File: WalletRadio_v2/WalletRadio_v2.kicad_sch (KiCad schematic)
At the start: 30 parts, among them Q1 BSP315P, Q2 Q_NPN_ECB, SW1 SW_SPDT, U3 LM324A

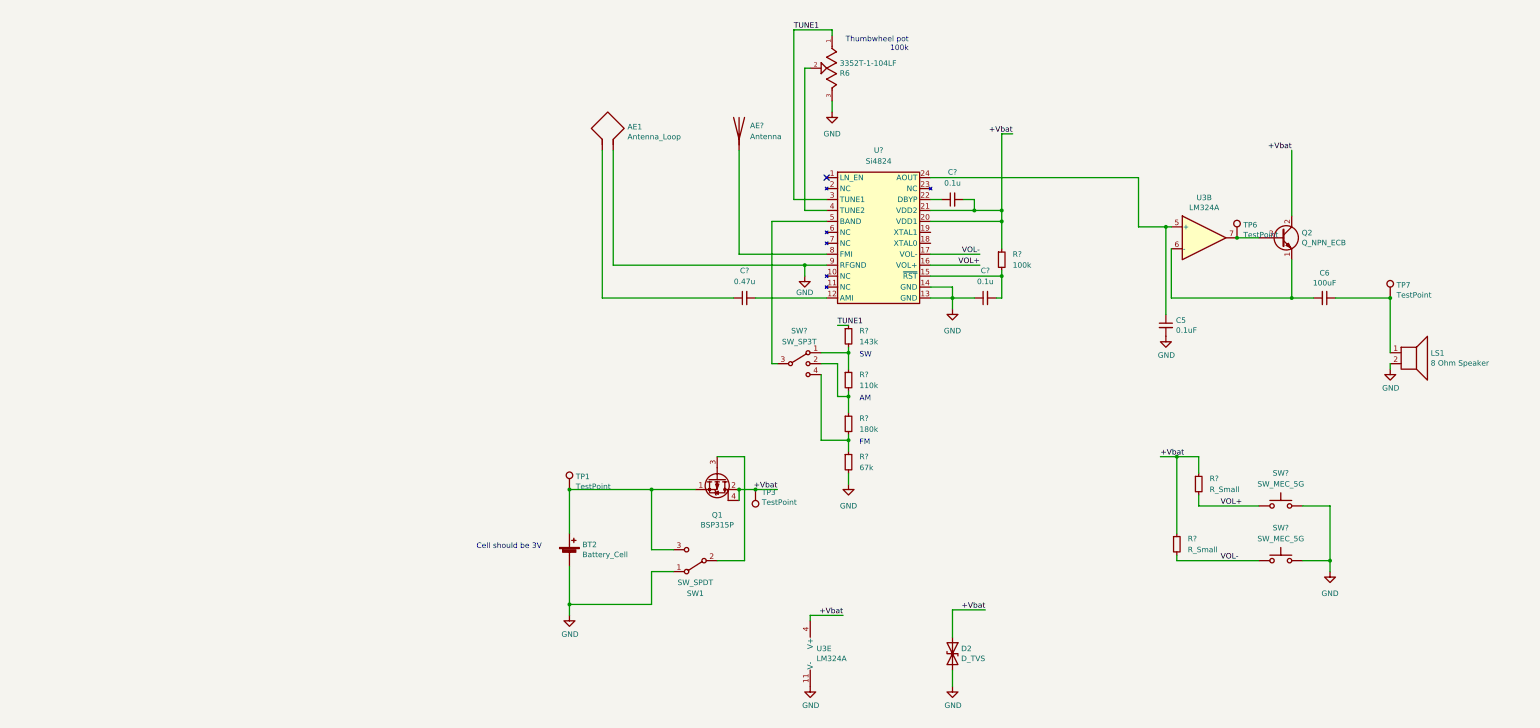
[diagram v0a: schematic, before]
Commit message: Changed the coin cell holder. Redid entire PCB layout
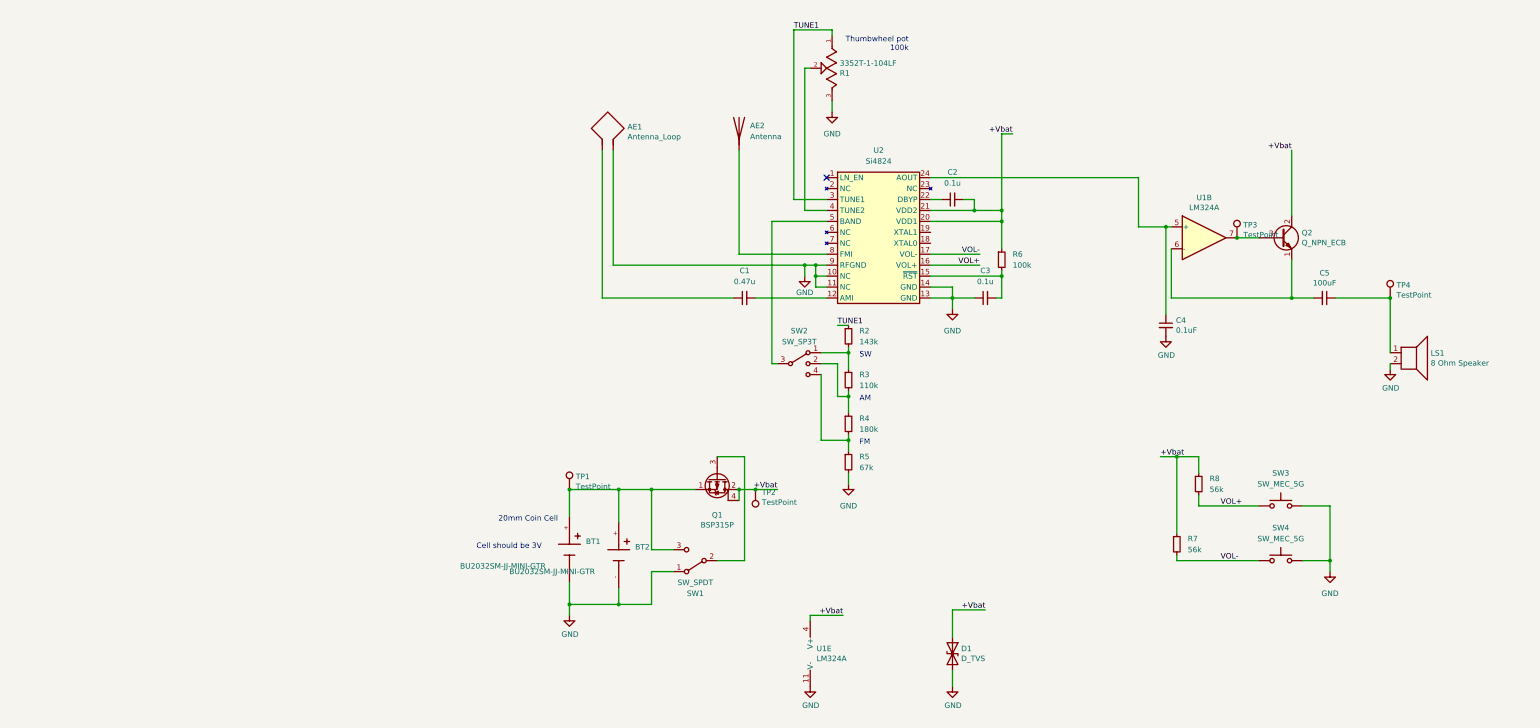
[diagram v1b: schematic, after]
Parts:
- removed BT2: Battery_Cell, WalletRadio:20mmCoinCell, symbol Device:Battery_Cell
- removed U?: Si4824, Package_SO:SSOP-24_3.9x8.7mm_P0.635mm, symbol Si4824:Si4824
- added BT1, BT2: BU2032SM-JJ-MINI-GTR, WalletRadio:BAT_BU2032SM-JJ-MINI-GTR, symbol WalletRadio_v2:BU2032SM-JJ-MINI-GTR
- added U2: Si4824, Package_SO:SSOP-24_3.9x8.7mm_P0.635mm, symbol Si4824:Si4824
- AE2: renamed from AE?; footprint (none) -> WalletRadio:FM_antenna
- C1, C3: renamed from C?; footprint (none) -> Capacitor_SMD:C_0603_1608Metric_Pad1.08x0.95mm_HandSolder
- C5: renamed from C6; footprint Resistor_SMD:R_0603_1608Metric_Pad1.05x0.95mm_HandSolder -> Capacitor_SMD:C_1206_3216Metric_Pad1.33x1.80mm_HandSolder
- R2, R3, R4, R5: renamed from R?; footprint (none) -> Resistor_SMD:R_0603_1608Metric_Pad0.98x0.95mm_HandSolder
- R7, R8: renamed from R?; value R_Small -> 56k
- gave numbers to parts that had none: 5
- renumbered C5 to C4, D2 to D1, R6 to R1, TP3 to TP2, TP6 to TP3, TP7 to TP4, U3 to U1
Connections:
- net +Vbat: now also U2.20 (VDD1), U2.21 (VDD2)
- net GND: now also BT1.-, BT2.-, U2.10 (NC), U2.11 (NC), U2.13 (GND), U2.14 (GND), U2.9 (RFGND)
- net TUNE1: now also U2.3 (TUNE1)
- net VOL+: now also U2.16 (VOL+)
- net VOL-: now also U2.17 (VOL-)
- net at C4.1, U1.5 (+): now also U2.24 (AOUT)
- net at Q1.1 (S), SW1.3 (C), TP1.1: now also BT1.+, BT2.+
- net at R1.2: now also U2.4 (TUNE2)
- net at C1.2: now also U2.12 (AMI)
- net at SW2.3: now also U2.5 (BAND)
- net at C2.1: now also U2.22 (DBYP)
- net at C3.2, R6.2: now also U2.15 (~{RST})
- net at AE2.1 (A): now also U2.8 (FMI)
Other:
- note added: "20mm Coin Cell"

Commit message: Added the remaining footprints for the components and continued laying out
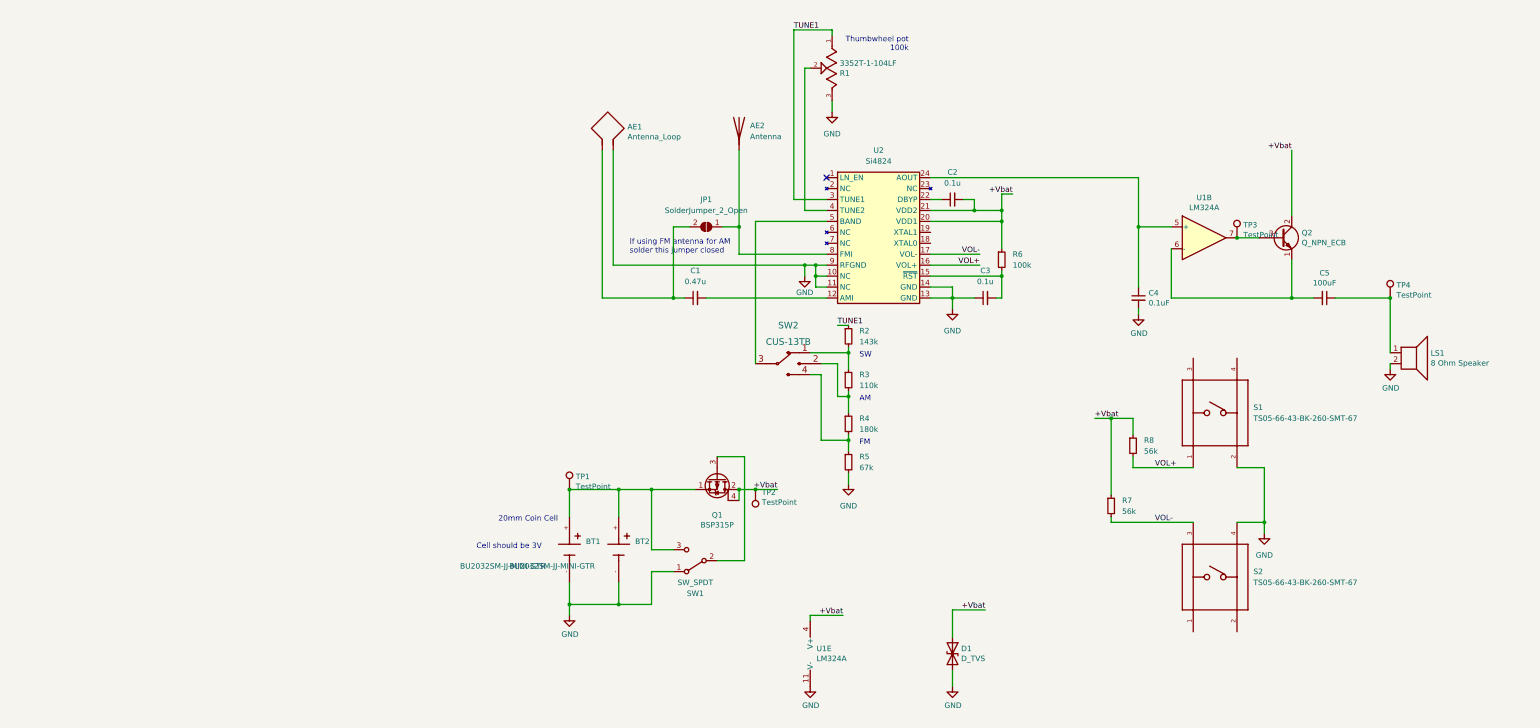
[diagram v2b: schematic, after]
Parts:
- removed SW2: SW_SP3T, symbol Switch:SW_SP3T
- removed SW3, SW4: SW_MEC_5G, symbol Switch:SW_MEC_5G
- added JP1: SolderJumper_2_Open, Jumper:SolderJumper-2_P1.3mm_Open_TrianglePad1.0x1.5mm, symbol Jumper:SolderJumper_2_Open
- added S1, S2: TS05-66-43-BK-260-SMT-67, SW_TS05-66-43-BK-260-SMT-67, symbol WalletRadio_v2:TS05-66-43-BK-260-SMT-67
- added SW2: CUS-13TB, WalletRadio:CUS-13TB, symbol WalletRadio_v2:CUS-13TB
- C2: footprint (none) -> Capacitor_SMD:C_0603_1608Metric_Pad1.08x0.95mm_HandSolder
- C4: footprint Capacitor_SMD:C_0603_1608Metric_Pad1.05x0.95mm_HandSolder -> Capacitor_SMD:C_0603_1608Metric_Pad1.08x0.95mm_HandSolder
- R6, R7, R8: footprint (none) -> Resistor_SMD:R_0603_1608Metric_Pad0.98x0.95mm_HandSolder
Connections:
- net GND: now also S1.2, S2.4
- net VOL+: now also S1.1
- net VOL-: now also S2.3
- net at AE1.1, C1.1: now also JP1.2 (B)
- net at R2.2, R3.1: now also SW2.1
- net at R3.2, R4.1: now also SW2.2
- net at U2.5 (BAND): now also SW2.3
- net at R4.2, R5.1: now also SW2.4
- net at AE2.1 (A), U2.8 (FMI): now also JP1.1 (A)
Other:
- note added: "If using FM antenna for AM solder this jumper closed"
- moved on the sheet: BT2, C1, C4, R7, R8

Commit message: Did more layout
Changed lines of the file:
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@@
       (effects (font (size 1.27 1.27)) (justify left bottom) hide)
     )
-    (property "DigiKey" "https://www.digikey.com/en/products/detail/BU2032SM-JJ-MINI-GTR/BU2032SM-JJ-MINI-GCT-ND/2647819?WT.z_cid=ref_netcomponents_dkc_buynow&utm_source=netcomponents&utm_medium=aggregator&utm_campaign=buynow" (id 10) (at 62.23 140.97 90)
-      (effects (font (size 1.27 1.27)) hide)
-    )
+    (property "DigiKey" "https://www.digikey.com/en/products/detail/BU2032SM-JJ-MINI-GTR/BU2032SM-JJ-MINI-GCT-ND/2647819?WT.z_cid=ref_netcomponents_dkc_buynow&utm_source=netcomponents&utm_medium=aggregator&utm_campaign=buynow" (id 10) (at 62.23 140.97 90))
     (pin "+")
     (pin "-")

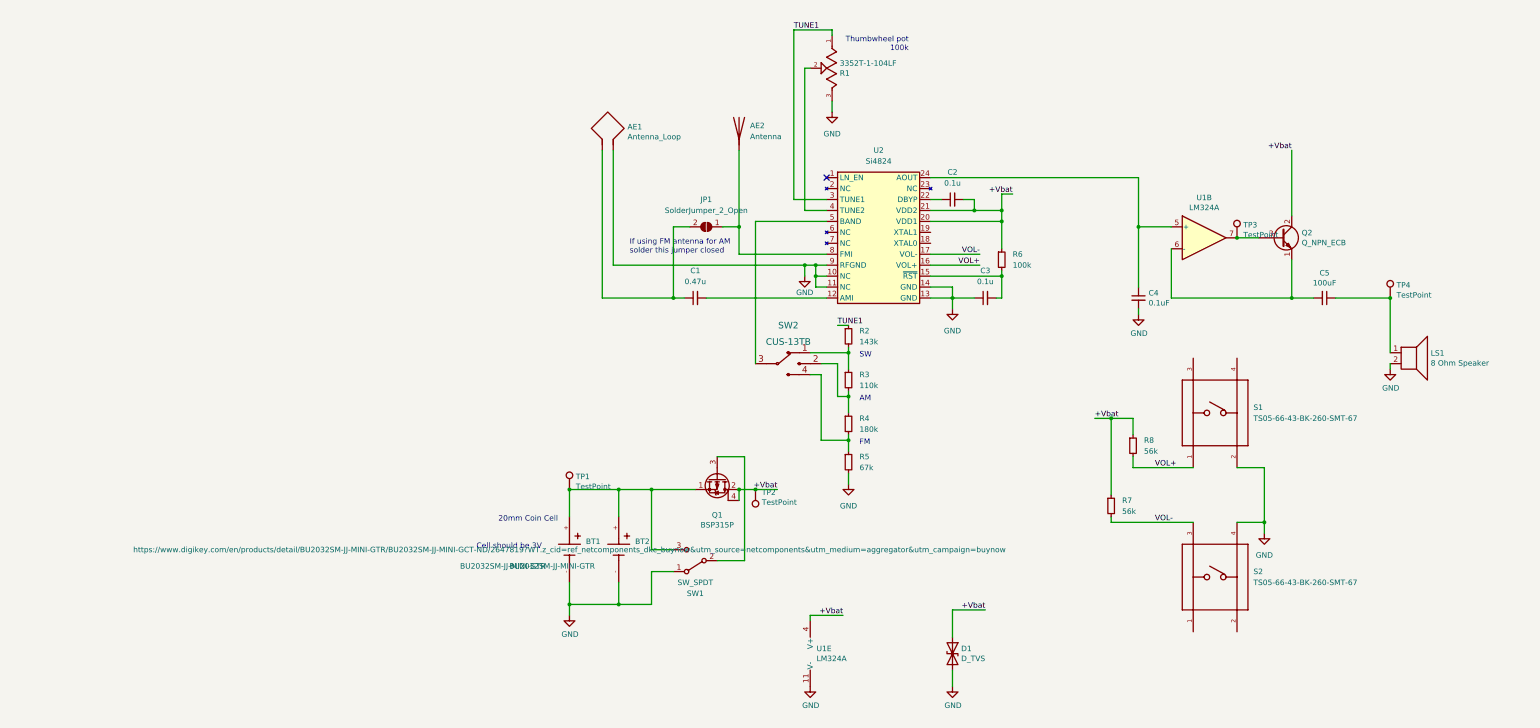
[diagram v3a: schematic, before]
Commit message: Switched to LiIon battery; rerouted, also added battery charger w/ USB-C
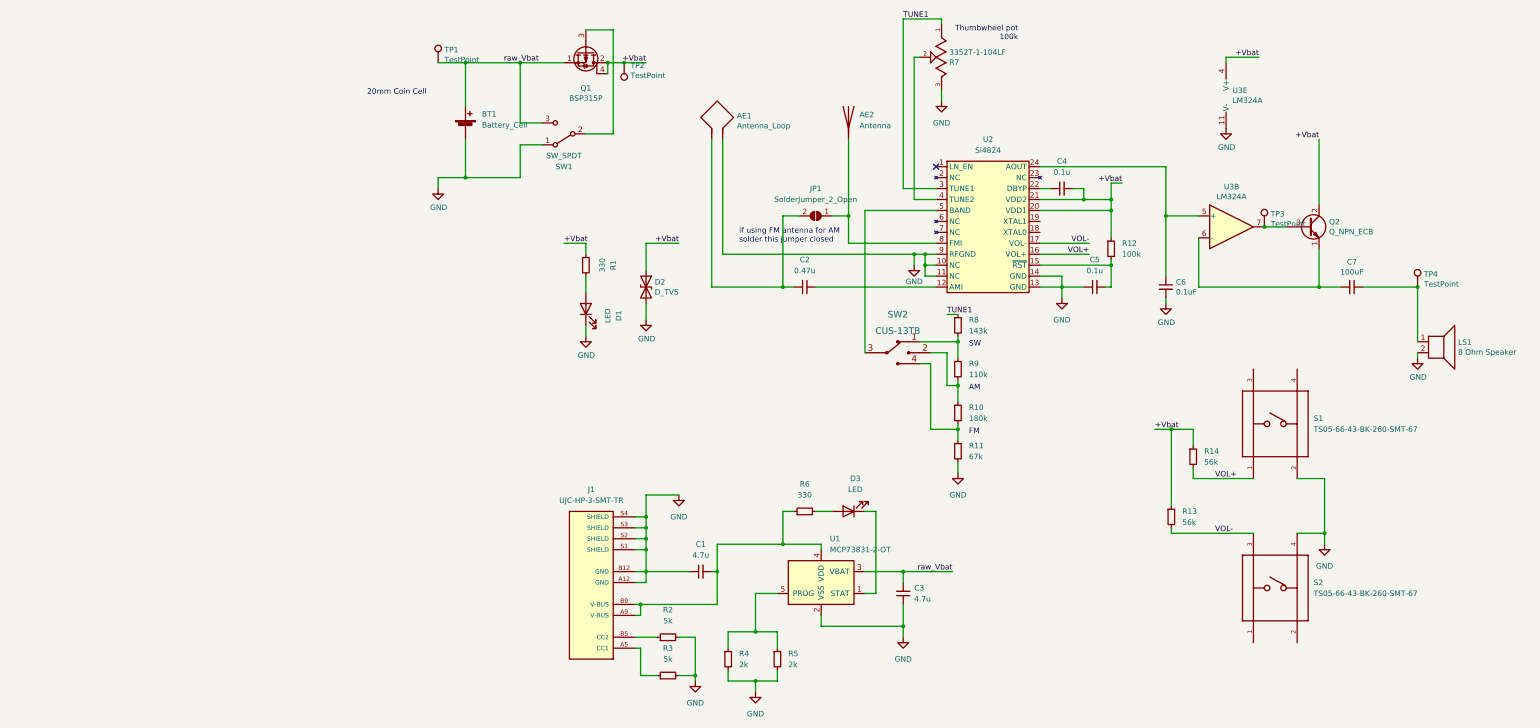
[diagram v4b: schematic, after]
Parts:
- removed BT1, BT2: BU2032SM-JJ-MINI-GTR, WalletRadio:BAT_BU2032SM-JJ-MINI-GTR, symbol WalletRadio_v2:BU2032SM-JJ-MINI-GTR
- added BT1: Battery_Cell, WalletRadio:1578_LiIon_Bat, symbol Device:Battery_Cell
- added C1, C3: 4.7u, Capacitor_SMD:C_0603_1608Metric_Pad1.08x0.95mm_HandSolder, symbol Device:C_Small
- added D1, D3: LED, symbol Device:LED
- added J1: UJC-HP-3-SMT-TR, WalletRadio:CUI_UJC-HP-3-SMT-TR, symbol WalletRadio_v2:UJC-HP-3-SMT-TR
- added R1, R6: 330, Resistor_SMD:R_0603_1608Metric_Pad0.98x0.95mm_HandSolder, symbol Device:R_Small
- added R2, R3: 5k, Resistor_SMD:R_0603_1608Metric_Pad0.98x0.95mm_HandSolder, symbol Device:R_Small
- added R4, R5: 2k, Resistor_SMD:R_0603_1608Metric_Pad0.98x0.95mm_HandSolder, symbol Device:R_Small
- added U1: MCP73831-2-OT, Package_TO_SOT_SMD:SOT-23-5, symbol Battery_Management:MCP73831-2-OT
- renumbered C1 to C2, C2 to C4, C3 to C5, C4 to C6, C5 to C7, D1 to D2, R4 to R10, R5 to R11, R6 to R12, R7 to R13, R8 to R14, R1 to R7, R2 to R8, R3 to R9, U1 to U3
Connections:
- net +Vbat: now also R1.1
- net GND: now also BT1.2 (-), C1.1, C3.1, D1.1 (K), J1.A12 (GND), J1.B12 (GND), J1.S1 (SHIELD), J1.S2 (SHIELD), J1.S3 (SHIELD), J1.S4 (SHIELD), R2.2, R3.2, R4.2, R5.2, U1.2 (VSS)
- net raw_Vbat: now reaches Q1.1 (S), SW1.3 (C), TP1.1
- net raw_Vbat: now also BT1.1 (+), C3.2, U1.3 (VBAT)
- new net: D3.1 (K), U1.1 (STAT)
- new net: C1.2, J1.A9 (V-BUS), J1.B9 (V-BUS), R6.1, U1.4 (VDD)
- new net: R4.1, R5.1, U1.5 (PROG)
- new net: J1.A5 (CC1), R3.1
- new net: J1.B5 (CC2), R2.1
- new net: D1.2 (A), R1.2
- new net: D3.2 (A), R6.2
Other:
- note removed: "Cell should be 3V"
- moved on the sheet: AE1, AE2, C2, C4, C5, C6, C7, D2, JP1, LS1, Q1, Q2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

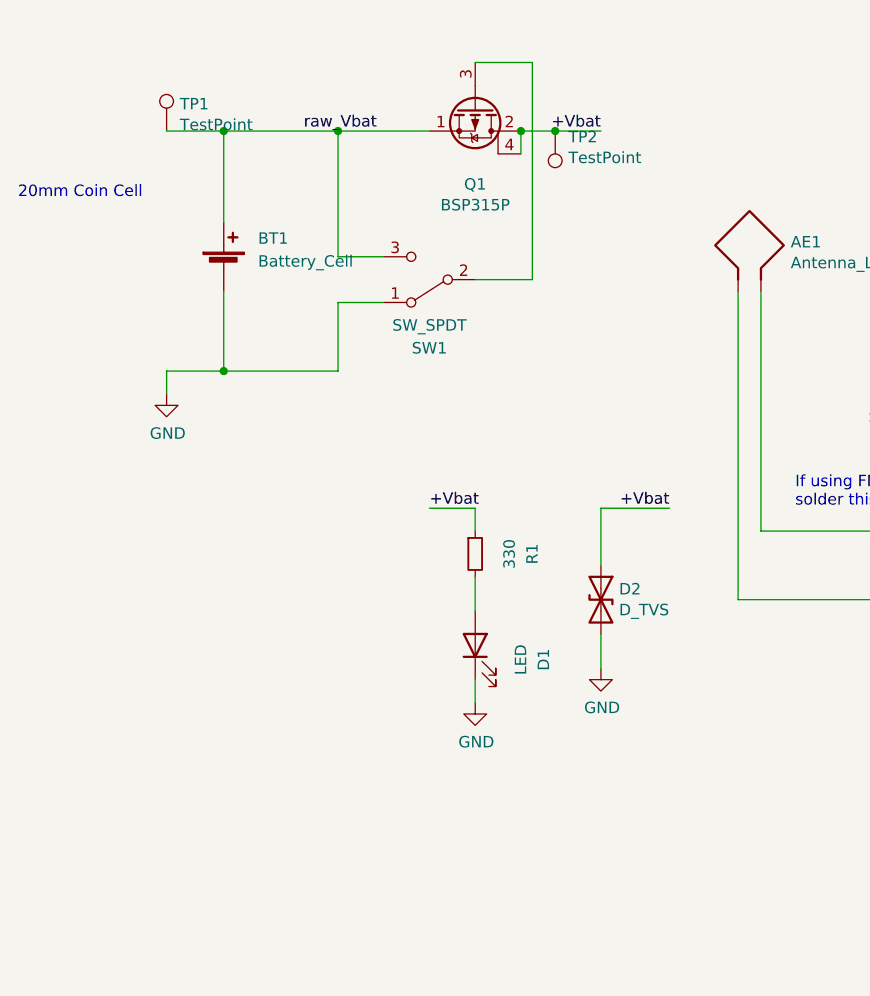
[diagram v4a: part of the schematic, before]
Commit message: Added a zener diode clamp to ensure max 3.3V operating voltage on power rail
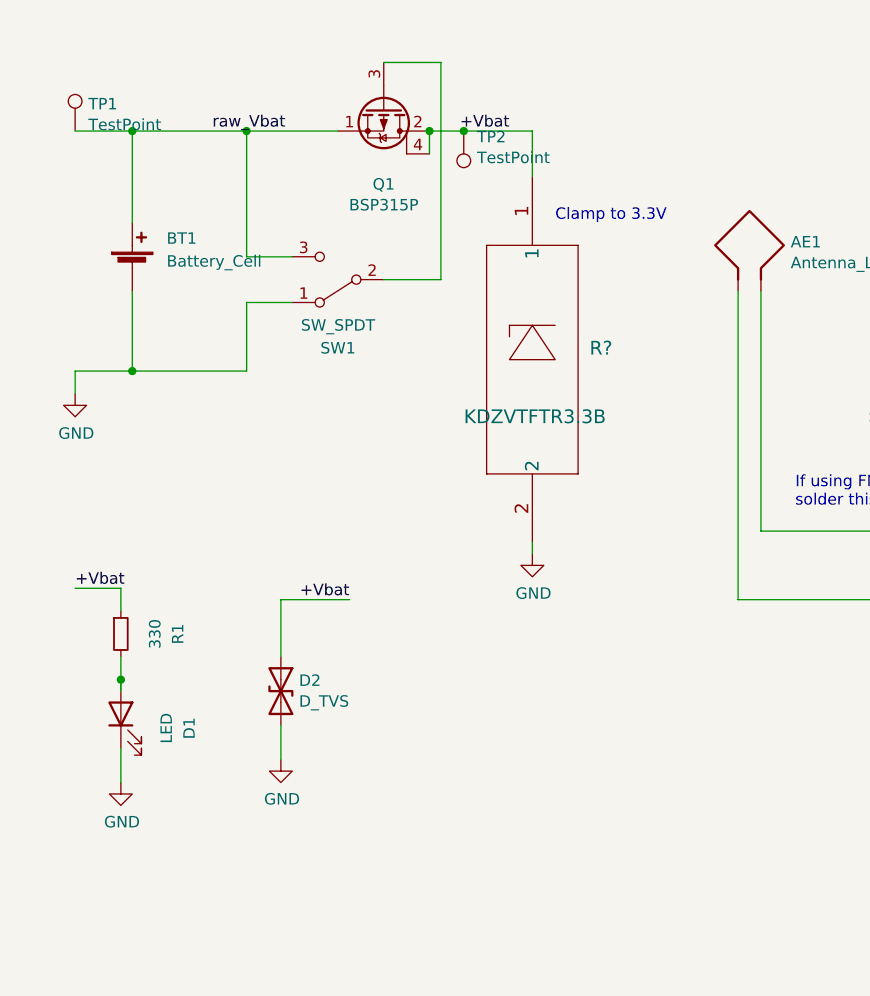
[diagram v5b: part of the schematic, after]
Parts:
- added R?: KDZVTFTR3.3B, WalletRadio:KDZVTFTR3.3B, symbol WalletRadio_v2:KDZVTFTR3.3B
- D1, D3: footprint (none) -> LED_SMD:LED_0603_1608Metric_Pad1.05x0.95mm_HandSolder
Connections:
- net +Vbat: now also R?.1
- net GND: now also R?.2
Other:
- note added: "Clamp to 3.3V"
- note removed: "20mm Coin Cell"
- moved on the sheet: BT1, D1, D2, Q1, R1, SW1, TP1, TP2

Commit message: Did more PCB layout.
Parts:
- removed R5: 2k, Resistor_SMD:R_0603_1608Metric_Pad0.98x0.95mm_HandSolder, symbol Device:R_Small
- gave numbers to parts that had none: 1
- renumbered R9 to R10, R10 to R11, R11 to R12, R12 to R13, R13 to R14, R14 to R15, R2 to R3, R3 to R4, R4 to R5, R6 to R7, R7 to R8, R8 to R9
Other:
- moved on the sheet: R5
